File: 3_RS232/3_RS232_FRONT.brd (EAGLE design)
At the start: 71.5 x 24 mm, 0 parts

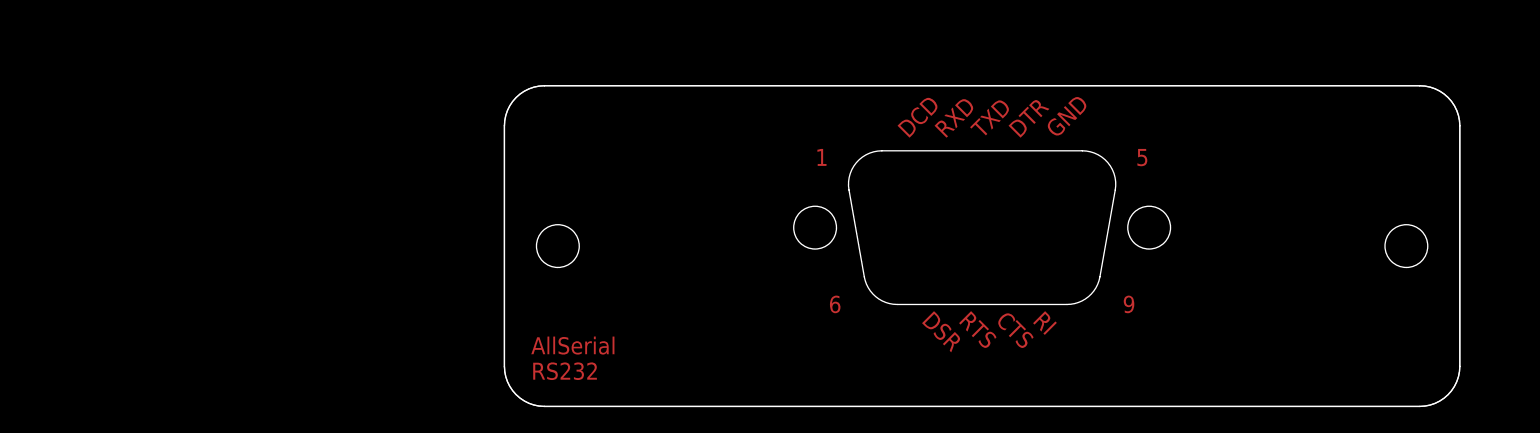
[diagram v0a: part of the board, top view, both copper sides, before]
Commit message: pro mini layout corrected
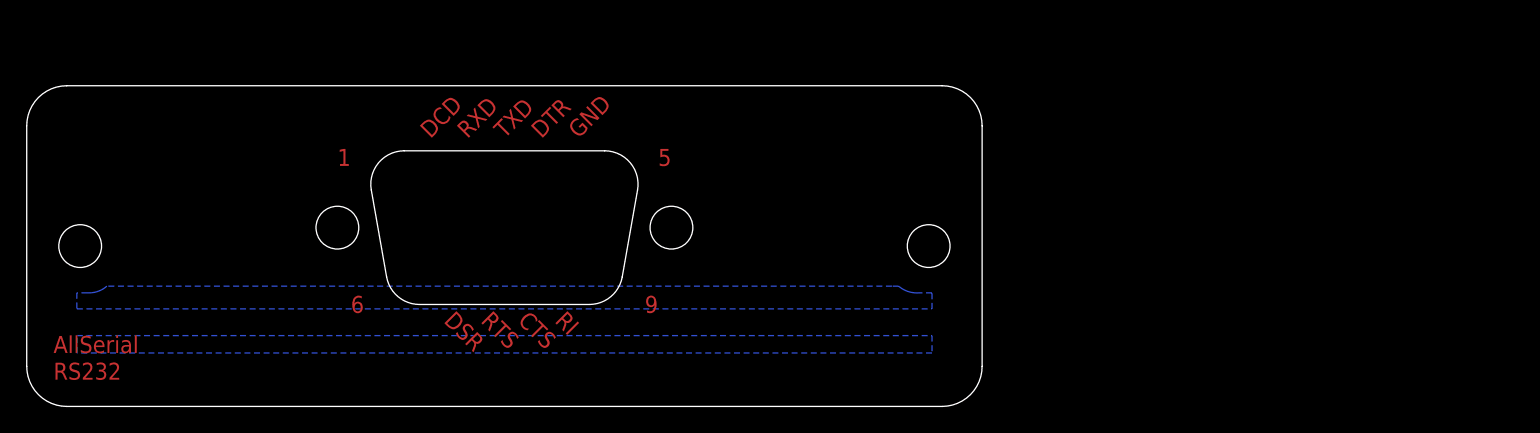
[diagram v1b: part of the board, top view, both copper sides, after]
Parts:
- added E$1: (no value), AllSerialv2:PANEL
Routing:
- added copper zone on layer 16, net S$1
- added copper zone on layer 16, net S$2
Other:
- outline, holes or cut-outs redrawn
- board text added: "RS232"
- board text removed: "AllSerial RS232"

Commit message: Cleanup, front with lib elements
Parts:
- removed E$1: (no value), AllSerialv2:PANEL
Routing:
- removed copper zone on layer 16, net S$1
- removed copper zone on layer 16, net S$2
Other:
- outline, holes or cut-outs redrawn
- board text added: "AllSerial RS232"
- board text removed: "RS232"
